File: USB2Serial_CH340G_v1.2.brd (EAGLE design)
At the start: 23.3 x 25.5 mm, 22 parts, among them CN1 UART, CN2 47346-0001, IC1 AMS1117-3.3, U2 FT232RL

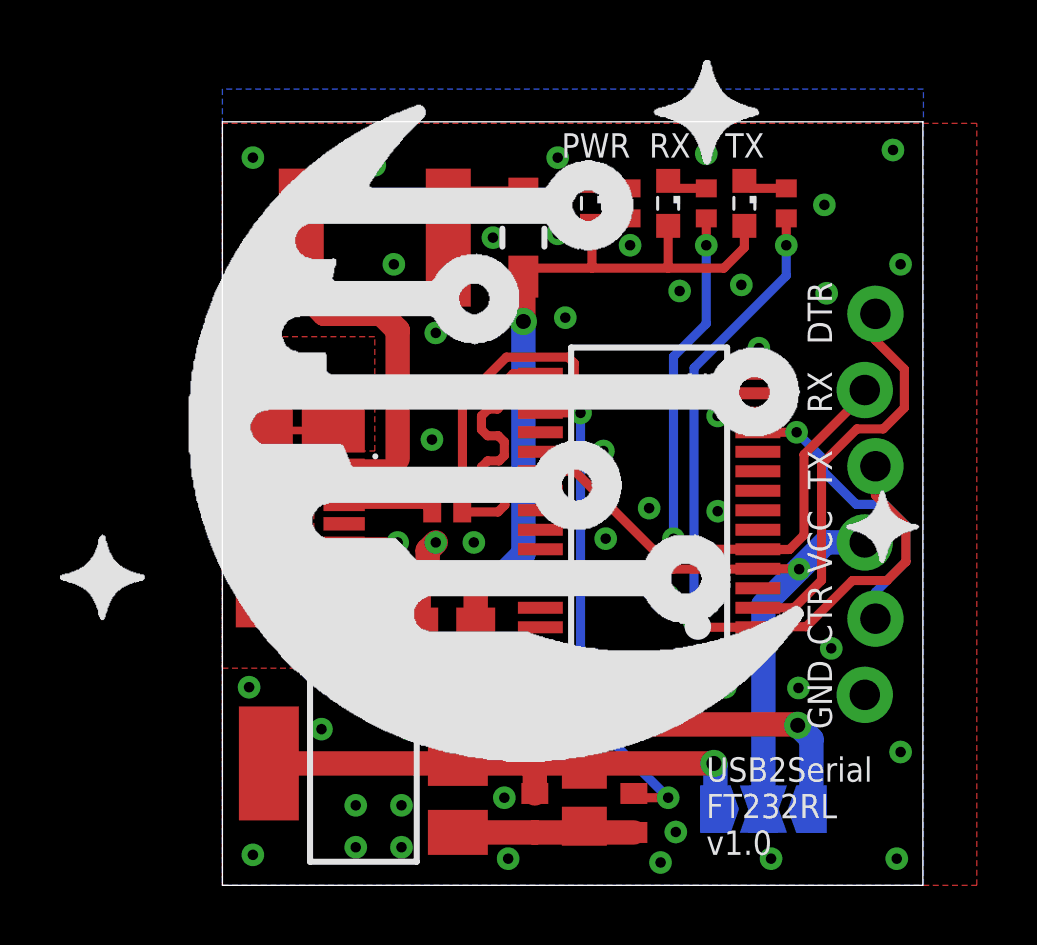
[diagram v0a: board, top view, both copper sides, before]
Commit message: Added C2. Added 1.2 for CH240G board.
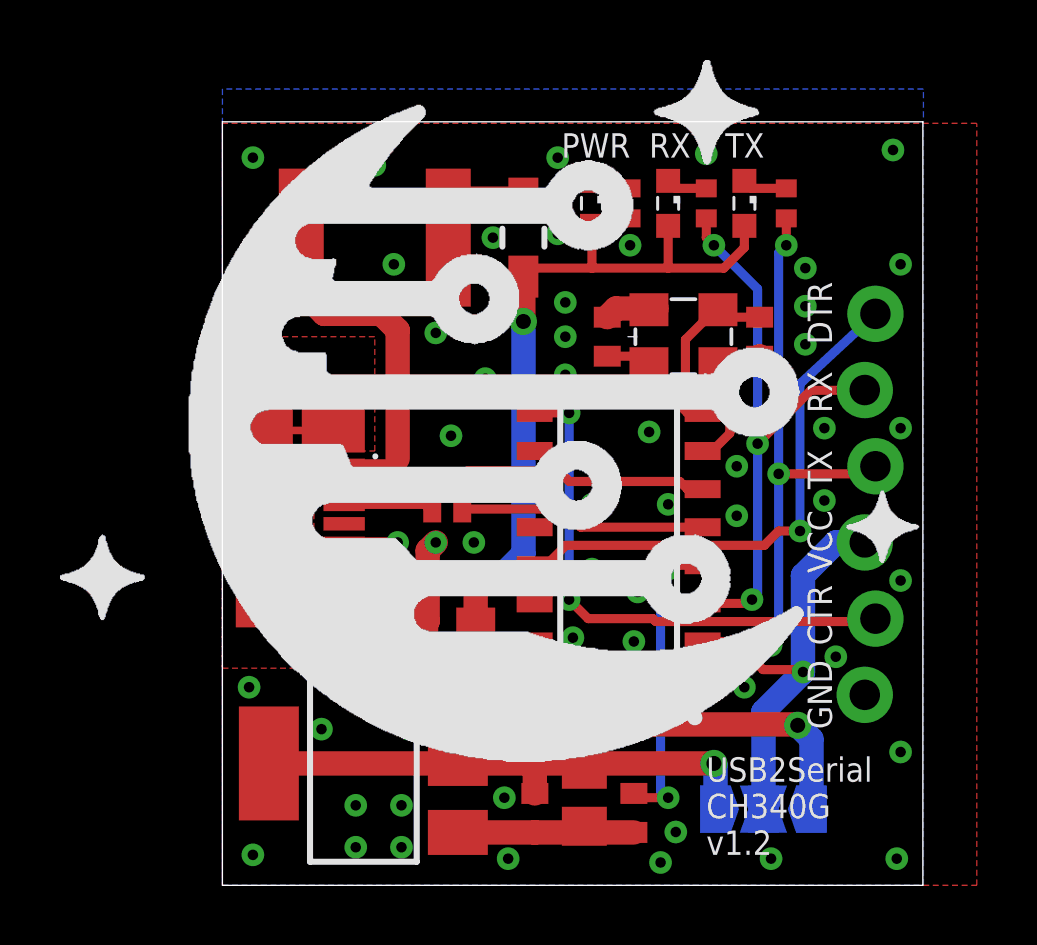
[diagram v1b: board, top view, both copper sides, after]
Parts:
- removed U2: FT232RL, ftdichip:SSOP28
- added C10, C9: 12pF, rcl:C0402
- added Q1: 12MHz, crystal-geyer_V1_0:3.2X2.5_KX-7
- added U1: CH340G, SparkFun-IC-Comms:SO016
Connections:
- new net USB_OSC_IN: C9.2, Q1.3, U1.7
- new net USB_OSC_OUT: C10.2, Q1.1, U1.8
- net GND: now also C10.1, C9.1, U1.1; no longer U2.18, U2.21, U2.25, U2.26, U2.7
- net N$6: now also U1.4; no longer U2.17
- net UART_CTS: now also U1.9; no longer U2.11
- net UART_DTR: now also U1.13; no longer U2.2
- net UART_RX: now also U1.3; no longer U2.5
- net UART_TX: now also U1.2; no longer U2.1
- net USB_D_M: now also U1.6; no longer U2.16
- net USB_D_P: now also U1.5; no longer U2.15
- net VCC: now also U1.16; no longer U2.20, U2.4
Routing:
- net USB_OSC_IN: track 0.00 -> 8.42 mm
- net UART_CTS: track 9.99 -> 17.9 mm, vias 1 -> 2
- net UART_TX: track 26.4 -> 20.1 mm, vias 2 -> 3
- net N$6: track 16.7 -> 10.5 mm
- net UART_DTR: track 13.4 -> 17.7 mm, vias 0 -> 1
- net USB_OSC_OUT: track 0.00 -> 4.17 mm
- net GND: track 13.2 -> 16.2 mm, vias 52 -> 59
- net UART_RX: track 21.5 -> 19.5 mm, vias 2 -> 3
- net VCC: track 21.0 -> 20.3 mm
- net USB_D_P: track 9.02 -> 8.31 mm
- net USB_D_M: track 9.01 -> 8.39 mm
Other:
- board text added: "USB2Serial CH340G v1.2"
- board text added: "USB2Serial CH340G v1.2 (c) Andriy Golovnya http://redscorp.net"
- board text removed: "USB2Serial FT232RL v1.0"
- board text removed: "USB2Serial FT232RL v1.0 (c) Andriy Golovnya http://redscorp.net"
